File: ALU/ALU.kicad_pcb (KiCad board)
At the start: 4 copper layers, 100 x 100 mm, 74 parts, among them IC1 SN74AHCT16245DGVR, J1 Conn_01x06_Pin, J2 Conn_02x15_Odd_Even, J3 Conn_02x15_Odd_Even, J4 Conn_02x15_Odd_Even, J5 Conn_01x01_Pin, J6 Conn_01x01_Pin, J7 Conn_01x01_Pin, J8 Conn_01x01_Pin, U1 74AHC1G08, U10 74HCT21, U11 74AHC1G32DBVR, U12 74AHCT1G02DBVR, U13 74AHCT1G08DBVR, U14 74AHCT1G08DBVR, U15 74AHC1G32DBVR, U16 74AHC1G32DBVR, U17 74AHC1G08, U18 SN74AHC16374DGGR, U19 74AHCT1G08DBVR, U2 SN74AHC16374DGGR, U20 74AHCT1G02DBVR, U21 74AHCT1G02DBVR, U3 74AHC1G04, U4 74LS181, U5 74LS181, U6 74AHCT1G08DBVR, U7 74HCT11, U8 74LS181, U9 74LS181

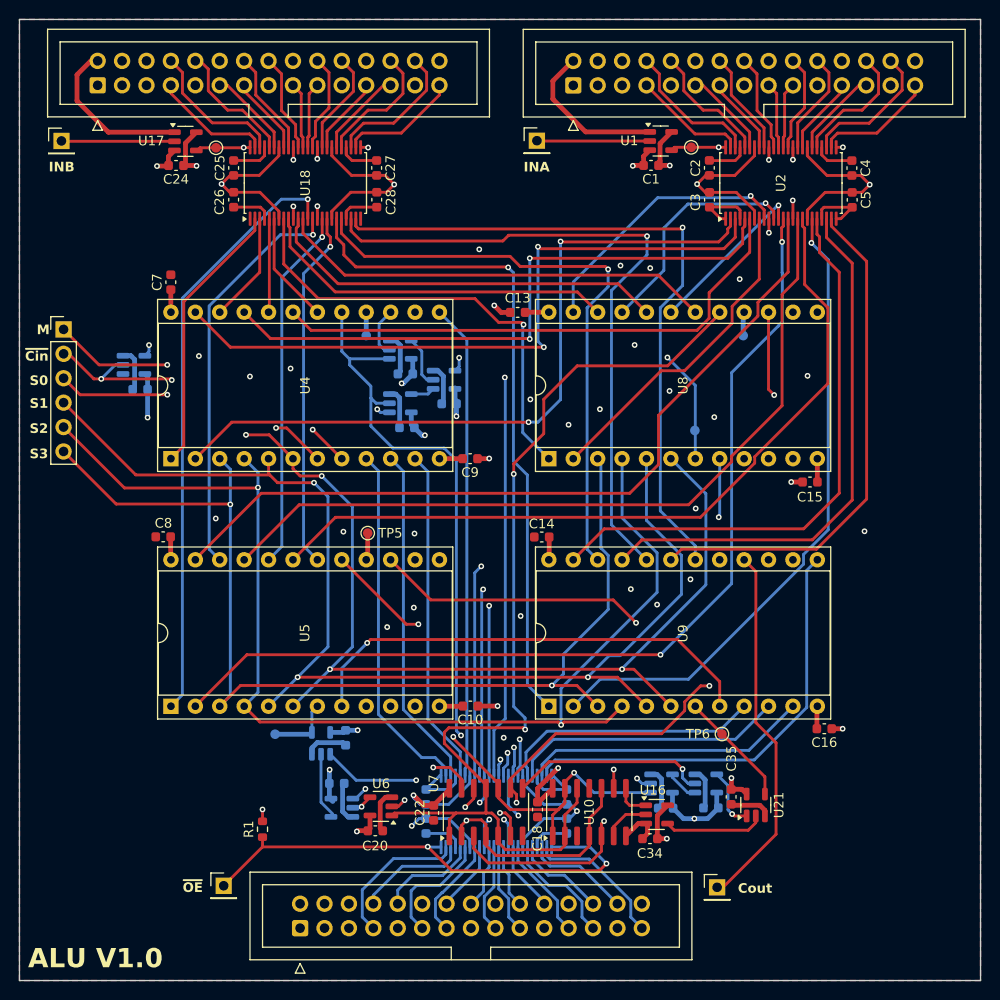
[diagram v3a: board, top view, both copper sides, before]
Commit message: Fixed ALU silkscreen for new fab
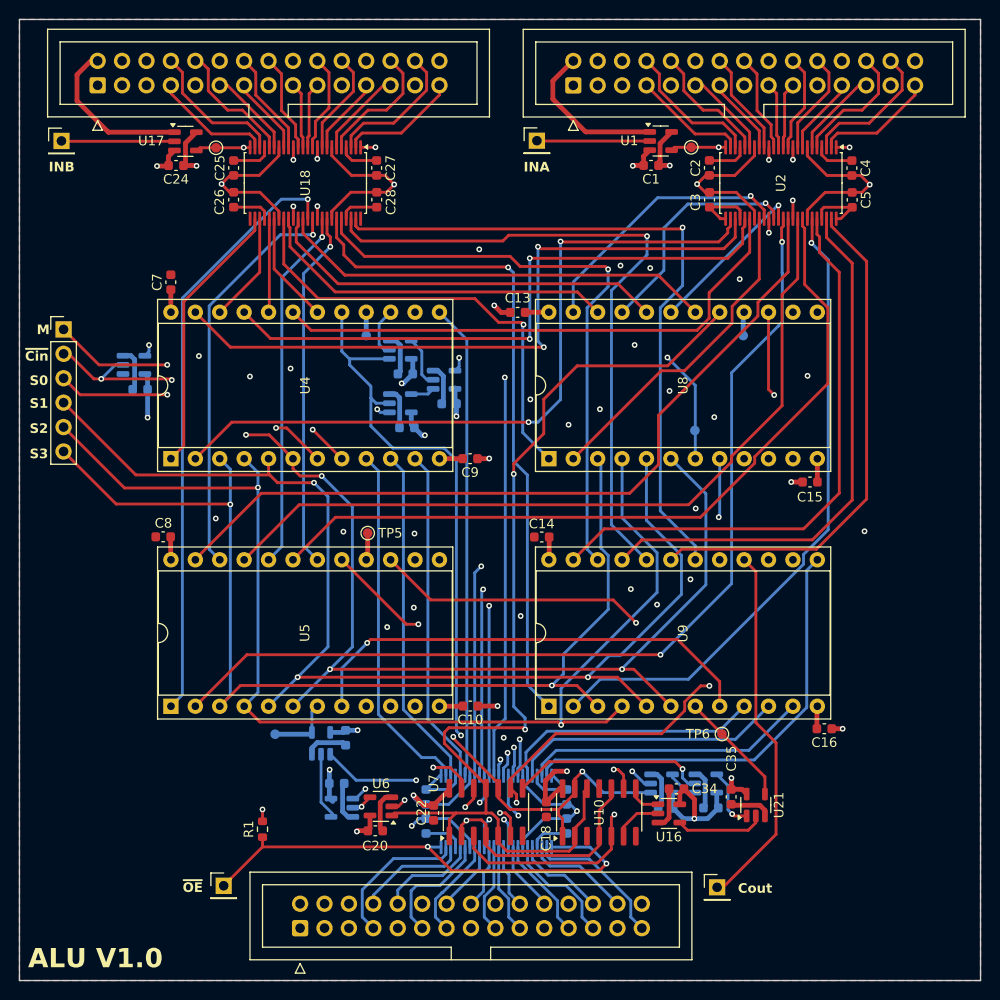
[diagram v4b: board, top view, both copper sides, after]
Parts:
- IC1: value SN74AHCT16245DGVR -> SN74AHCT16245DGGR
- U18, U2: value SN74AHC16374DGGR -> SN74AHCT16374DGGR
- U3: value 74AHC1G04 -> 74AHC1G04DBVR
- moved C34 5.88 mm to (202.4, 94.0)
- moved U16 1.28 mm to (201.6, 96.6)
- moved U10 1.03 mm to (194.3, 96.5)
- moved C18 0.91 mm to (188.8, 96.2)
- turned U18 to -90 degrees
- turned U2 to -90 degrees
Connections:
- TP1 pad 1: Net-(U2-1CLK) -> Net-(U2-1~{OE})
- TP2 pad 1: Net-(U18-1CLK) -> Net-(U18-1~{OE})
- U1 pad 4: Net-(U2-1CLK) -> Net-(U2-1~{OE})
- U17 pad 4: Net-(U18-1CLK) -> Net-(U18-1~{OE})
- U18 pad 1: GND -> Net-(U18-1~{OE})
- U18 pad 11: /INB/DOUT6 -> /INB/DIN9
- U18 pad 12: /INB/DOUT7 -> /INB/DIN8
- U18 pad 13: /INB/DOUT8 -> /INB/DIN7
- U18 pad 14: /INB/DOUT9 -> /INB/DIN6
- U18 pad 16: /INB/DOUT10 -> /INB/DIN5
- U18 pad 17: /INB/DOUT11 -> /INB/DIN4
- U18 pad 19: /INB/DOUT12 -> /INB/DIN3
- U18 pad 2: /INB/DOUT0 -> /INB/DIN15
- U18 pad 20: /INB/DOUT13 -> /INB/DIN2
- U18 pad 22: /INB/DOUT14 -> /INB/DIN1
- U18 pad 23: /INB/DOUT15 -> /INB/DIN0
- U18 pad 24: GND -> Net-(U18-1~{OE})
- U18 pad 25: Net-(U18-1CLK) -> GND
- U18 pad 26: /INB/DIN15 -> /INB/DOUT0
- U18 pad 27: /INB/DIN14 -> /INB/DOUT1
- U18 pad 29: /INB/DIN13 -> /INB/DOUT2
- U18 pad 3: /INB/DOUT1 -> /INB/DIN14
- U18 pad 30: /INB/DIN12 -> /INB/DOUT3
- U18 pad 32: /INB/DIN11 -> /INB/DOUT4
- U18 pad 33: /INB/DIN10 -> /INB/DOUT5
- U18 pad 35: /INB/DIN9 -> /INB/DOUT6
- U18 pad 36: /INB/DIN8 -> /INB/DOUT7
- U18 pad 37: /INB/DIN7 -> /INB/DOUT8
- U18 pad 38: /INB/DIN6 -> /INB/DOUT9
- U18 pad 40: /INB/DIN5 -> /INB/DOUT10
- U18 pad 41: /INB/DIN4 -> /INB/DOUT11
- U18 pad 43: /INB/DIN3 -> /INB/DOUT12
- U18 pad 44: /INB/DIN2 -> /INB/DOUT13
- U18 pad 46: /INB/DIN1 -> /INB/DOUT14
- U18 pad 47: /INB/DIN0 -> /INB/DOUT15
- U18 pad 48: Net-(U18-1CLK) -> GND
- U18 pad 5: /INB/DOUT2 -> /INB/DIN13
- U18 pad 6: /INB/DOUT3 -> /INB/DIN12
- U18 pad 8: /INB/DOUT4 -> /INB/DIN11
- U18 pad 9: /INB/DOUT5 -> /INB/DIN10
- U2 pad 1: GND -> Net-(U2-1~{OE})
- U2 pad 11: /INA/DOUT6 -> /INA/DIN9
- U2 pad 12: /INA/DOUT7 -> /INA/DIN8
- U2 pad 13: /INA/DOUT8 -> /INA/DIN7
- U2 pad 14: /INA/DOUT9 -> /INA/DIN6
- U2 pad 16: /INA/DOUT10 -> /INA/DIN5
- U2 pad 17: /INA/DOUT11 -> /INA/DIN4
- U2 pad 19: /INA/DOUT12 -> /INA/DIN3
- U2 pad 2: /INA/DOUT0 -> /INA/DIN15
- U2 pad 20: /INA/DOUT13 -> /INA/DIN2
- U2 pad 22: /INA/DOUT14 -> /INA/DIN1
- U2 pad 23: /INA/DOUT15 -> /INA/DIN0
- U2 pad 24: GND -> Net-(U2-1~{OE})
- U2 pad 25: Net-(U2-1CLK) -> GND
- U2 pad 26: /INA/DIN15 -> /INA/DOUT0
- U2 pad 27: /INA/DIN14 -> /INA/DOUT1
- U2 pad 29: /INA/DIN13 -> /INA/DOUT2
- U2 pad 3: /INA/DOUT1 -> /INA/DIN14
- U2 pad 30: /INA/DIN12 -> /INA/DOUT3
- U2 pad 32: /INA/DIN11 -> /INA/DOUT4
- U2 pad 33: /INA/DIN10 -> /INA/DOUT5
- U2 pad 35: /INA/DIN9 -> /INA/DOUT6
- U2 pad 36: /INA/DIN8 -> /INA/DOUT7
- U2 pad 37: /INA/DIN7 -> /INA/DOUT8
- U2 pad 38: /INA/DIN6 -> /INA/DOUT9
- U2 pad 40: /INA/DIN5 -> /INA/DOUT10
- U2 pad 41: /INA/DIN4 -> /INA/DOUT11
- U2 pad 43: /INA/DIN3 -> /INA/DOUT12
- U2 pad 44: /INA/DIN2 -> /INA/DOUT13
- U2 pad 46: /INA/DIN1 -> /INA/DOUT14
- U2 pad 47: /INA/DIN0 -> /INA/DOUT15
- U2 pad 48: Net-(U2-1CLK) -> GND
- U2 pad 5: /INA/DOUT2 -> /INA/DIN13
- U2 pad 6: /INA/DOUT3 -> /INA/DIN12
- U2 pad 8: /INA/DOUT4 -> /INA/DIN11
- U2 pad 9: /INA/DOUT5 -> /INA/DIN10
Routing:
- net Net-(U18-1~{OE}): track 0.00 -> 20.9 mm, vias 0 -> 2
- net Net-(U2-1~{OE}): track 0.00 -> 20.8 mm, vias 0 -> 2
- net Net-(U2-1CLK): track 19.4 -> 0.00 mm, vias 2 -> 0
- net Net-(U18-1CLK): track 19.4 -> 0.00 mm, vias 2 -> 0
- net /alu16/Y2: track 57.0 -> 55.0 mm
- net Net-(U16-Pad4): track 10.7 -> 9.45 mm
- net /alu16/Y1: track 107.6 -> 108.7 mm
- net +5V: track 176.6 -> 177.7 mm, vias 25 -> 24
- net /alu16/Y0: track 92.4 -> 93.4 mm
- net /alu16/carry generator/Cin: track 98.0 -> 98.7 mm

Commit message: Fixed silkscreen on ALU and Double Buffer
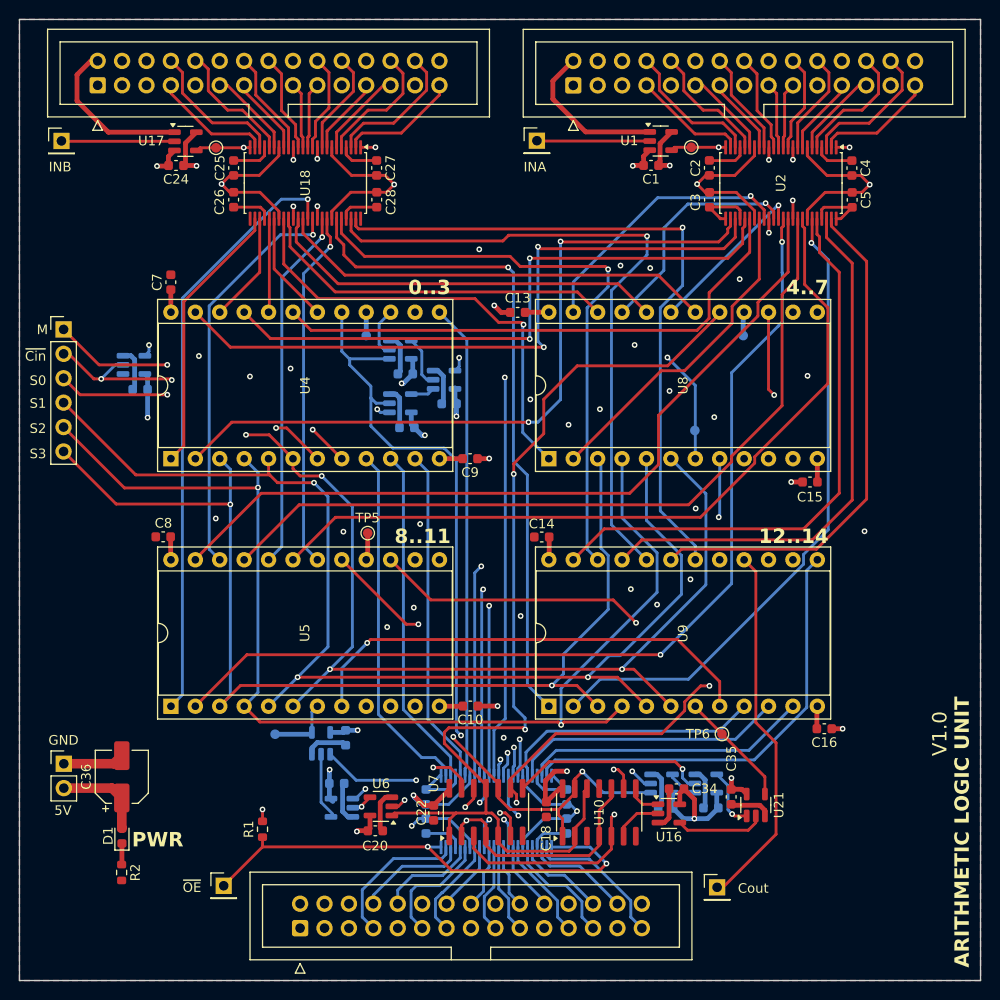
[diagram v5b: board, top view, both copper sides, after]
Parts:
- added C36: 100uF, Capacitor_SMD:CP_Elec_5x5.3, F.Cu at (144.7, 92.8)
- added D1: LED, LED_SMD:LED_0603_1608Metric, F.Cu at (144.7, 98.9)
- added J9: Conn_01x02, Connector_PinHeader_2.54mm:PinHeader_1x02_P2.54mm_Vertical, F.Cu at (138.6, 91.4)
- added R2: 100, Resistor_SMD:R_0603_1608Metric, F.Cu at (144.6, 102.8)
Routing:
- net +5V: track 177.7 -> 187.3 mm
- net GND: track 149.9 -> 156.3 mm
- net Net-(D1-K): track 0.00 -> 2.22 mm
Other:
- board text added: "0..3"
- board text added: "12..14"
- board text added: "4..7"
- board text added: "5V"
- board text added: "8..11"
- board text added: "ARITHMETIC LOGIC UNIT"
- board text added: "GND"
- board text added: "PWR"
- board text added: "V1.0"
- board text removed: "ALU V1.0"
